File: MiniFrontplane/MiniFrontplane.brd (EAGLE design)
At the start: 99.1 x 39.4 mm, 17 parts, among them IC2 74ACT14N, U1 MCP130SOT

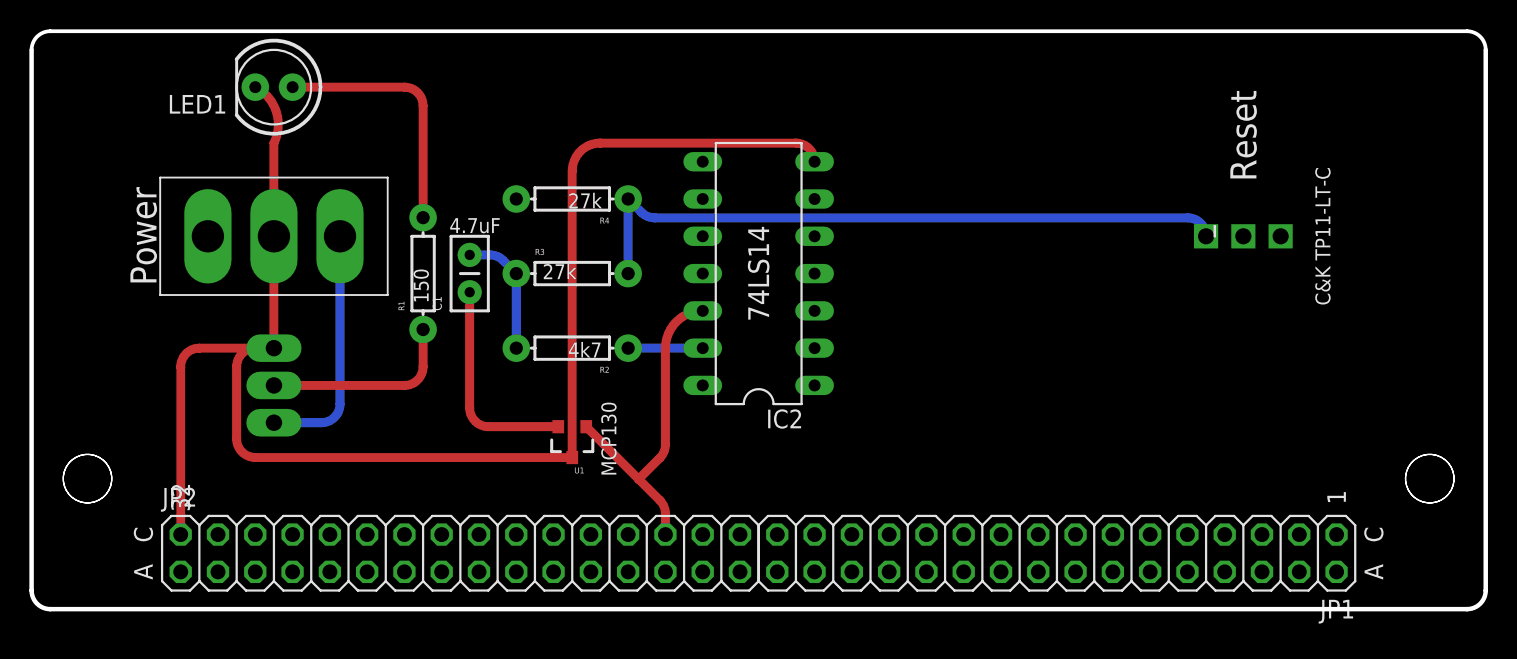
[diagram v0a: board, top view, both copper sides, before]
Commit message: Fixed fit between backplane & enclosure
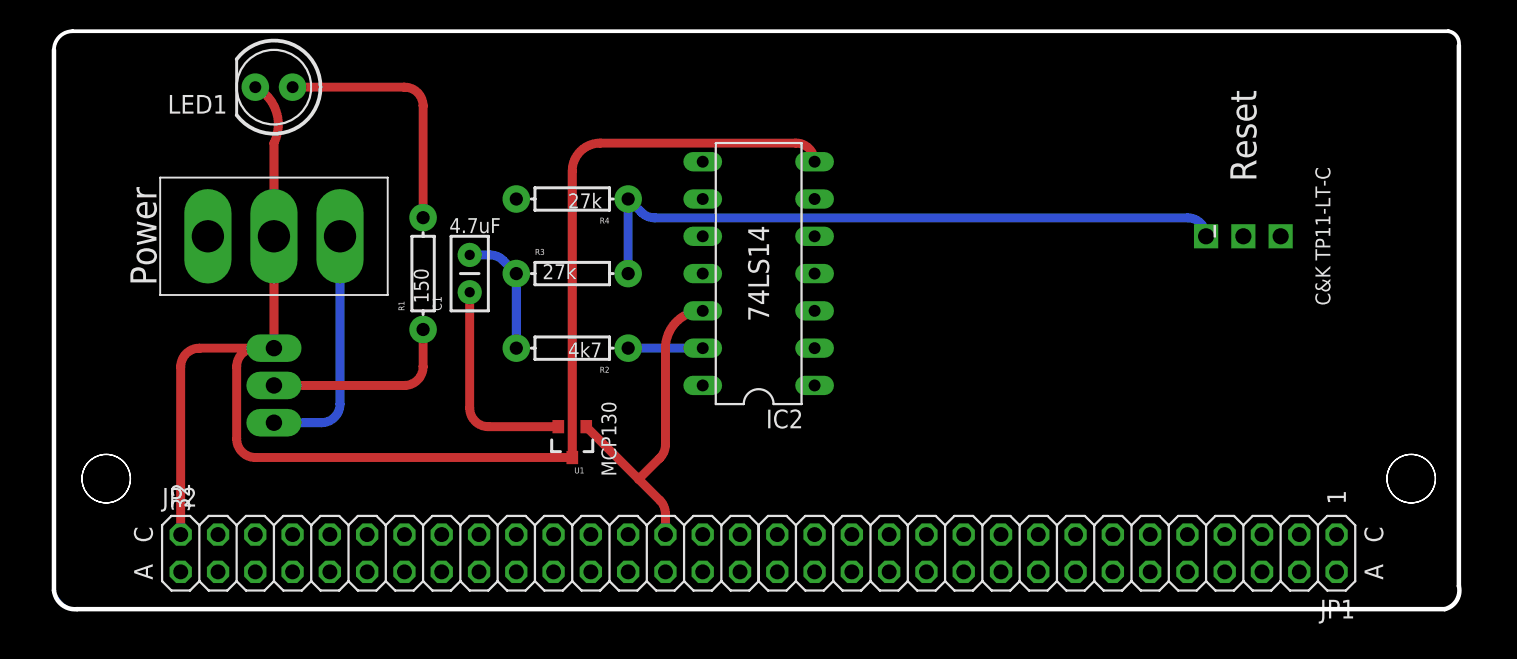
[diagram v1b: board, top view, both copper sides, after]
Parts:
- moved U$11 1.27 mm to (94.8, 10.3)
- moved U$9 1.27 mm to (94.8, 10.3)
- moved U$10 1.27 mm to (5.93, 10.3)
- moved U$12 1.27 mm to (5.93, 10.3)
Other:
- board size 99.1 x 39.4 mm -> 95.7 x 39.4 mm
- board text removed: "Benchoff13"
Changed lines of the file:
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@@
 <board>
 <plain>
-<wire x1="0.8468375" y1="39.535021875" x2="2.1168375" y2="40.805021875" width="0.254" layer="46" curve="-90"/>
-<wire x1="2.1168375" y1="40.805021875" x2="98.6368375" y2="40.805021875" width="0.254" layer="46"/>
-<wire x1="98.6368375" y1="40.805021875" x2="99.9068375" y2="39.535021875" width="0.254" layer="46" curve="-90"/>
-<wire x1="2.1168375" y1="1.435021875" x2="98.6368375" y2="1.435021875" width="0.3048" layer="46"/>
-<wire x1="98.6368375" y1="1.435021875" x2="99.9068375" y2="2.705021875" width="0.3048" layer="46" curve="90"/>
-<wire x1="99.9068375" y1="2.705021875" x2="99.9068375" y2="39.535021875" width="0.3048" layer="46"/>
-<wire x1="2.1168375" y1="1.435021875" x2="0.8468375" y2="2.705021875" width="0.3048" layer="46" curve="-90"/>
-<wire x1="0.8468375" y1="2.705021875" x2="0.8468375" y2="39.535021875" width="0.3048" layer="46"/>
+<wire x1="2.3708375" y1="39.535021875" x2="3.6408375" y2="40.805021875" width="0.254" layer="46" curve="-90"/>
+<wire x1="3.6408375" y1="40.805021875" x2="97.3668375" y2="40.805021875" width="0.254" layer="46"/>
+<wire x1="97.3668375" y1="40.805021875" x2="98.0780375" y2="39.839821875" width="0.254" layer="46" curve="-90"/>
+<wire x1="3.9456375" y1="1.435021875" x2="97.1128375" y2="1.435021875" width="0.3048" layer="46"/>
+<wire x1="97.1128375" y1="1.435021875" x2="98.0780375" y2="3.009821875" width="0.3048" layer="46" curve="90"/>
+<wire x1="98.0780375" y1="3.009821875" x2="98.0780375" y2="39.839821875" width="0.3048" layer="46"/>
+<wire x1="3.9456375" y1="1.435021875" x2="2.3708375" y2="2.705021875" width="0.3048" layer="46" curve="-90"/>
+<wire x1="2.3708375" y1="2.705021875" x2="2.3708375" y2="39.535021875" width="0.3048" layer="46"/>
 <text x="8.4668375" y="6.515021875" size="1.27" layer="21" font="vector" ratio="15" rot="R90" align="center">C</text>
 <text x="8.4668375" y="3.975021875" size="1.27" layer="21" font="vector" ratio="15" rot="R90" align="center">A</text>
@@
 <text x="89.323546875" y="26.835021875" size="1.016" layer="21" font="vector" ratio="15" rot="R90" align="bottom-center">C&amp;K TP11-LT-C</text>
 <rectangle x1="81.02549375" y1="27.0947375" x2="81.8713125" y2="27.2639" layer="21" rot="R90"/>
-<text x="91.44" y="3.81" size="1.016" layer="22" rot="MR180">Benchoff13</text>
 </plain>
 <attributes>
@@
 </autorouter>
 <elements>
-<element name="U$9" library="SparkFun-Electromechanical" package="STAND-OFF" value="" x="96.0968375" y="10.325021875" rot="MR90"/>
-<element name="U$10" library="SparkFun-Electromechanical" package="STAND-OFF" value="" x="4.6568375" y="10.325021875" rot="MR90"/>
-<element name="U$11" library="SparkFun-Electromechanical" package="STAND-OFF" value="" x="96.0968375" y="10.325021875" rot="MR90"/>
-<element name="U$12" library="SparkFun-Electromechanical" package="STAND-OFF" value="" x="4.6568375" y="10.325021875" rot="MR90"/>
+<element name="U$9" library="SparkFun-Electromechanical" package="STAND-OFF" value="" x="94.8268375" y="10.325021875" rot="MR90"/>
+<element name="U$10" library="SparkFun-Electromechanical" package="STAND-OFF" value="" x="5.9268375" y="10.325021875" rot="MR90"/>
+<element name="U$11" library="SparkFun-Electromechanical" package="STAND-OFF" value="" x="94.8268375" y="10.325021875" rot="MR90"/>
+<element name="U$12" library="SparkFun-Electromechanical" package="STAND-OFF" value="" x="5.9268375" y="10.325021875" rot="MR90"/>
 <element name="JP2" library="pinhead" package="2X16" value="" x="30.0568375" y="5.245021875"/>
 <element name="JP1" library="pinhead" package="2X16" value="" x="70.6968375" y="5.245021875" rot="R180"/>
@@
 <wire x1="17.3568375" y1="26.835021875" x2="17.3568375" y2="19.215021875" width="0.6096" layer="1"/>
 <polygon width="0.254" layer="1">
-<vertex x="0.8468375" y="2.705021875"/>
-<vertex x="0.8468375" y="39.535021875" curve="-90"/>
-<vertex x="2.1168375" y="40.805021875"/>
-<vertex x="98.6368375" y="40.805021875" curve="-90"/>
-<vertex x="99.9068375" y="39.535021875"/>
-<vertex x="99.9068375" y="2.705021875" curve="-90"/>
-<vertex x="98.6368375" y="1.435021875"/>
-<vertex x="2.1168375" y="1.435021875" curve="-90"/>
+<vertex x="2.3708375" y="2.705021875"/>
+<vertex x="2.3708375" y="39.535021875" curve="-90"/>
+<vertex x="3.6408375" y="40.805021875"/>
+<vertex x="97.3668375" y="40.805021875" curve="-90"/>
+<vertex x="98.0780375" y="39.535021875"/>
+<vertex x="98.0780375" y="2.705021875" curve="-90"/>
+<vertex x="97.1128375" y="1.435021875"/>
+<vertex x="4.5552375" y="1.435021875" curve="-90"/>
 </polygon>
 <contactref element="R4" pad="P$2"/>
@@
 <contactref element="IC2" pad="14"/>
 <polygon width="0.254" layer="16">
-<vertex x="0.8468375" y="2.705021875"/>
-<vertex x="0.8468375" y="39.535021875" curve="-90"/>
-<vertex x="2.1168375" y="40.805021875"/>
-<vertex x="98.6368375" y="40.805021875" curve="-90"/>
-<vertex x="99.9068375" y="39.535021875"/>
-<vertex x="99.9068375" y="2.705021875" curve="-90"/>
-<vertex x="98.6368375" y="1.435021875"/>
-<vertex x="2.1168375" y="1.435021875" curve="-90"/>
+<vertex x="2.4216375" y="3.975021875"/>
+<vertex x="2.4216375" y="39.535021875" curve="-90"/>
+<vertex x="3.6916375" y="40.805021875"/>
+<vertex x="97.3668375" y="40.805021875" curve="-90"/>
+<vertex x="98.0780375" y="39.535021875"/>
+<vertex x="98.0780375" y="2.705021875" curve="-90"/>
+<vertex x="97.1128375" y="1.435021875"/>
+<vertex x="3.6916375" y="1.435021875" curve="-90"/>
 </polygon>
 <contactref element="C1" pad="1"/>
